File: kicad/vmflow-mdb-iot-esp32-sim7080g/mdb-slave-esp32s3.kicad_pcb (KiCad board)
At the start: 2 copper layers, 58.4 x 41 mm, 41 parts, among them J1 MDB_Connector, J2 USB_C_Receptacle_USB2.0_16P, J3 Conn_02x11_Odd_Even, J4 JAE_SIM_Card_SF72S006, SW1 SW_Push, U1 TLP785, U2 SIM7080G, U3 ESP32-S3FH4R2, U4 TLP785, U5 LM2594HVM-3.3, Y1 Crystal_GND24

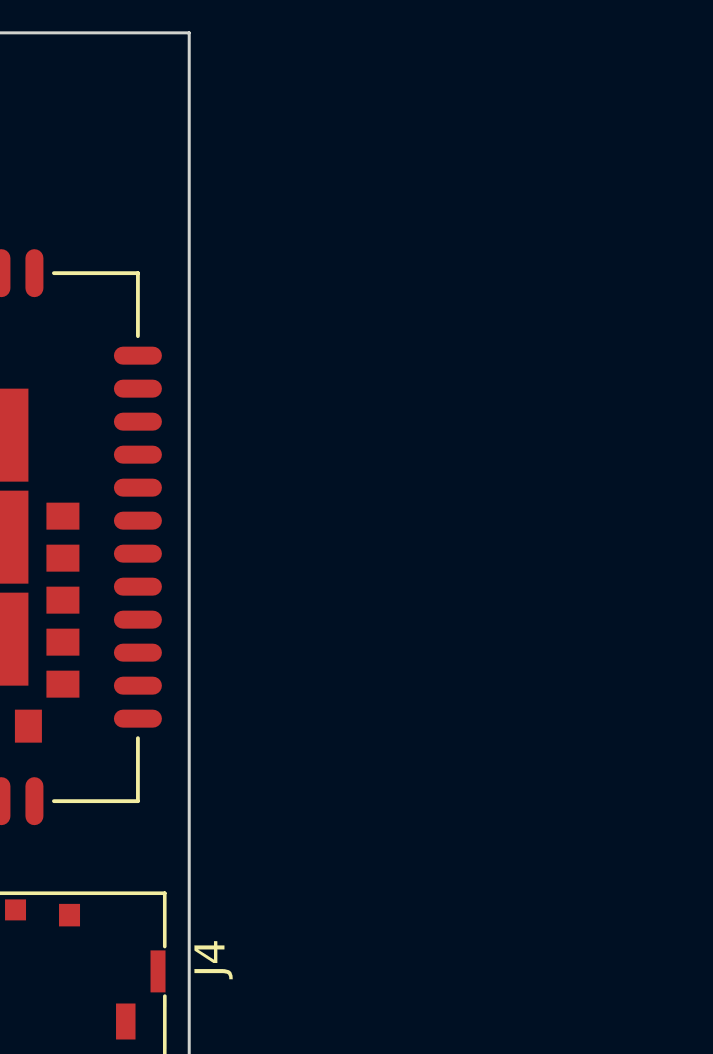
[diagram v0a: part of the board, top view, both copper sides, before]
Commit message: Connecting power wire
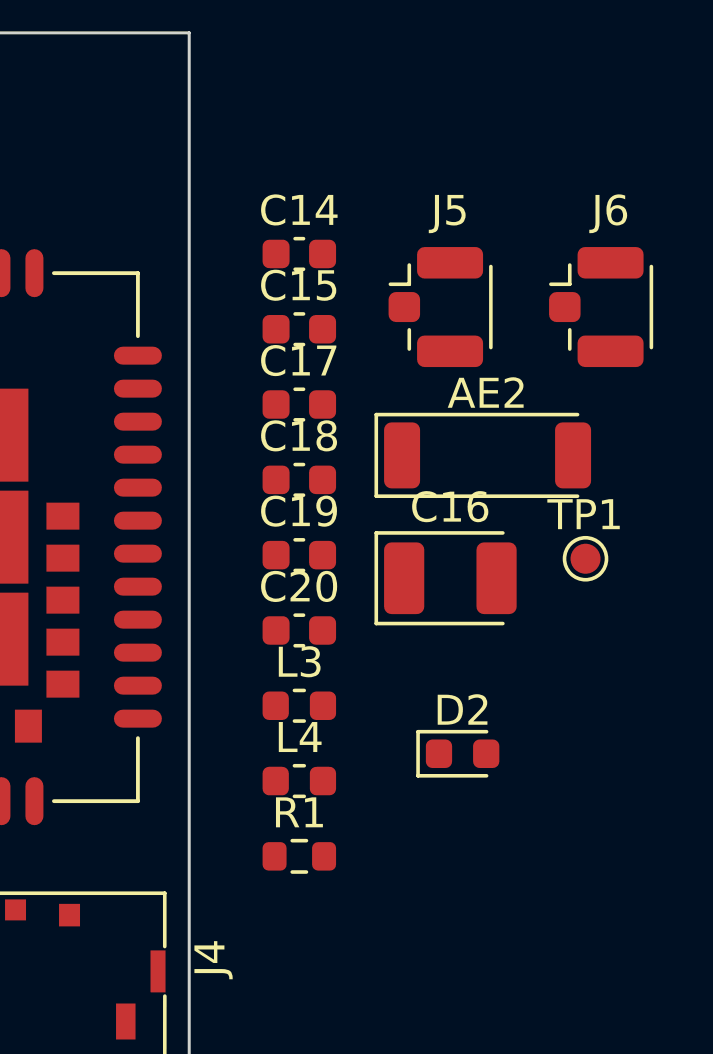
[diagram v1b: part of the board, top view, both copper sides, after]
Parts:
- added AE2: Antenna, RF_Antenna:Johanson_2450AT43F0100, F.Cu at (236.8, 97.2)
- added C14: 0.1uF, Capacitor_SMD:C_0603_1608Metric, F.Cu at (230.6, 90.5)
- added C15: 1uF, Capacitor_SMD:C_0603_1608Metric, F.Cu at (230.6, 93.0)
- added C16: 10uF, Capacitor_Tantalum_SMD:CP_EIA-3528-21_Kemet-B, F.Cu at (235.6, 101.3)
- added C17: 1.8pf, Capacitor_SMD:C_0603_1608Metric, F.Cu at (230.6, 95.5)
- added C18: 1.8pf, Capacitor_SMD:C_0603_1608Metric, F.Cu at (230.6, 98.0)
- added C19: 1.8pf, Capacitor_SMD:C_0603_1608Metric, F.Cu at (230.6, 100.5)
- added C20: 1.8pf, Capacitor_SMD:C_0603_1608Metric, F.Cu at (230.6, 103.0)
- added D2: LED, LED_SMD:LED_0603_1608Metric, F.Cu at (236.0, 107.1)
- added J5: Conn_Coaxial, Connector_Coaxial:U.FL_Hirose_U.FL-R-SMT-1_Vertical, F.Cu at (235.1, 92.2)
- added J6: Conn_Coaxial, Connector_Coaxial:U.FL_Hirose_U.FL-R-SMT-1_Vertical, F.Cu at (240.5, 92.2)
- added L3: 2.4nh, Inductor_SMD:L_0603_1608Metric, F.Cu at (230.6, 105.5)
- added L4: 2.4nh, Inductor_SMD:L_0603_1608Metric, F.Cu at (230.6, 108.0)
- added R1: 1k, Resistor_SMD:R_0603_1608Metric, F.Cu at (230.6, 110.5)
- added TP1: TestPoint, TestPoint:TestPoint_Pad_D1.0mm, F.Cu at (240.1, 100.6)
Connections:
- U2 pad 1: unconnected-(U2-UART1_TXD-Pad1) -> /io18
- U2 pad 2: unconnected-(U2-UART1_RXD-Pad2) -> /io17
- U2 pad 32: unconnected-(U2-RF_ANT-Pad32) -> /rf_ant
- U2 pad 34: VBAT -> +3V3
- U2 pad 35: VBAT -> +3V3
- U2 pad 39: unconnected-(U2-PWRKEY-Pad39) -> /io14
- U2 pad 41: unconnected-(U2-NETLIGHT-Pad41) -> /netlight
- U2 pad 42: unconnected-(U2-STATUS-Pad42) -> Net-(U2-STATUS)
- U2 pad 68: unconnected-(U2-GNSS_ANT-Pad68) -> /gnss_ant
